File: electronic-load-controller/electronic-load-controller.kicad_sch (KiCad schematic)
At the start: 64 parts, among them J1 Conn_01x04, J2 Conn_01x02, J3 Conn_01x05, J4 Conn_01x03, J5 Conn_01x04, J7 Conn_01x03, J8 Conn_01x03, Q1 BSS84, Q2 BSS138, Q3 BCP56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

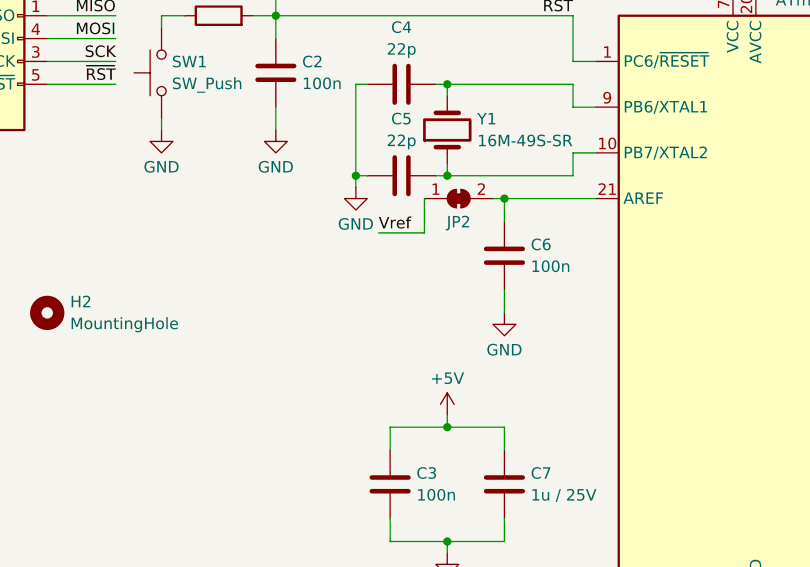
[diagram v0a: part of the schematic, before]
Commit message: Add lowpass filter to ADC
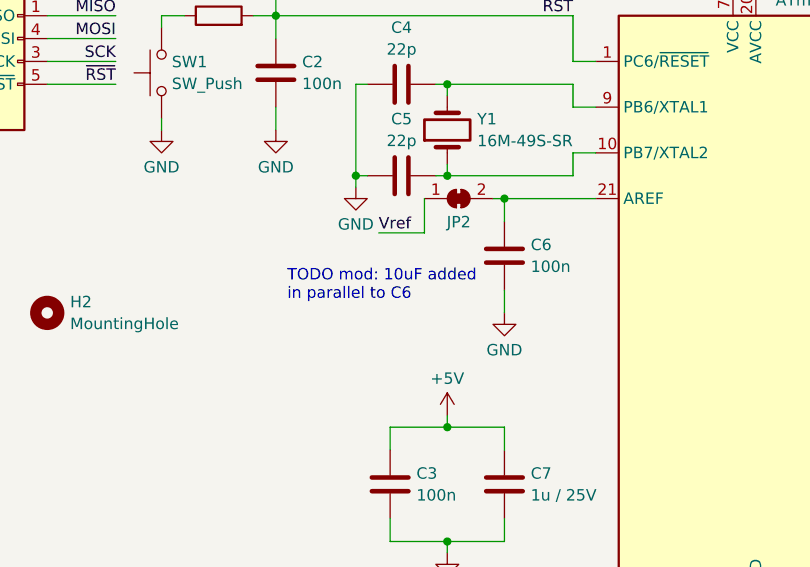
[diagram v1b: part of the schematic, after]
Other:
- note added: "TODO mod: 10uF added in parallel to C6"
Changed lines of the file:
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@@
     (stroke (width 0) (type default))
+  )
+  (text "TODO mod: 10uF added\nin parallel to C6" (at 77.47 62.23 0)
+    (effects (font (size 1.27 1.27)) (justify left bottom))
   )
   (text "Connect ISENSE to LM258N output\non analog board" (at 140.97 195.58 0)

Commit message: Add KiCAD PDF outputs
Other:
- note added: "TODO mod: 10uF added in parallel with C6"
- note removed: "TODO mod: 10uF added in parallel to C6"
- moved on the sheet: J8
